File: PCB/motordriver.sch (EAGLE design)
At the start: 52 parts, among them IC1 7818TV

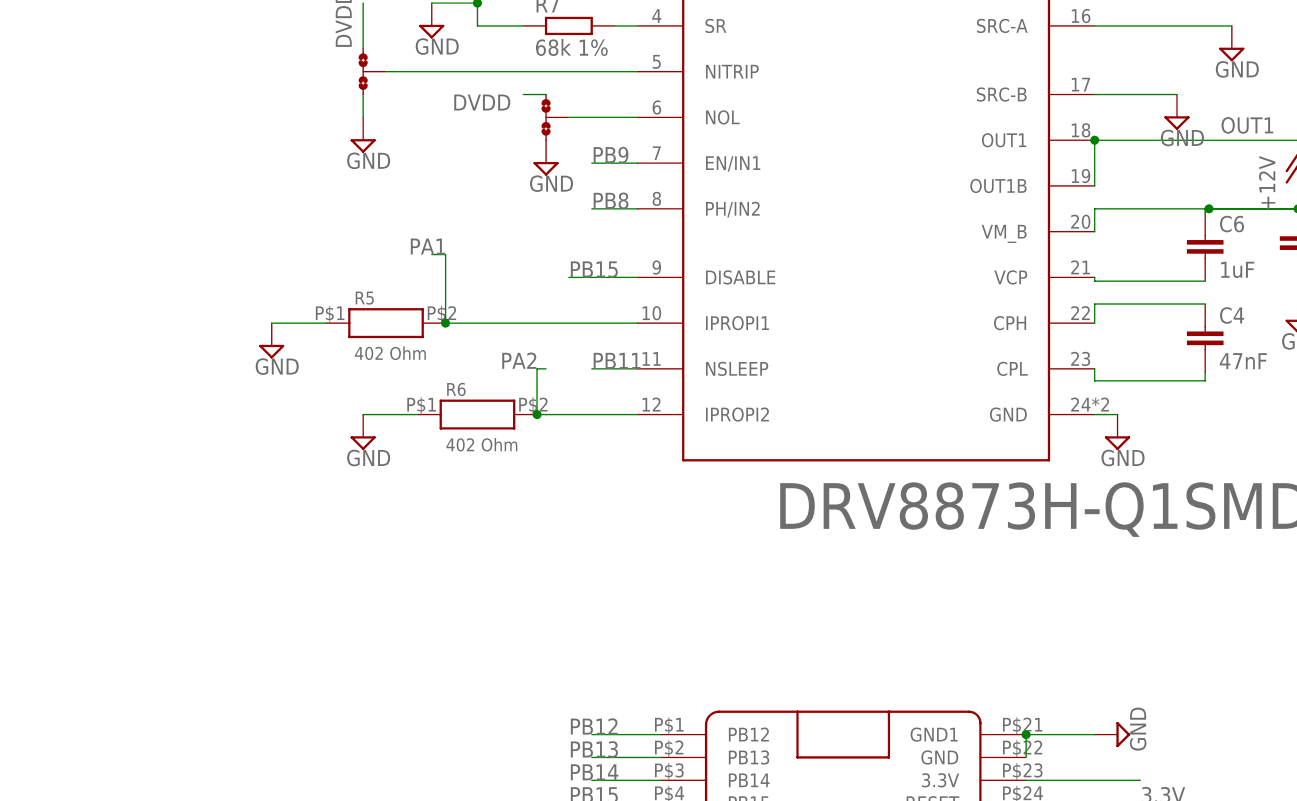
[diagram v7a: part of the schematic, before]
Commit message: added Low pass rc filter for the IOPROPx output
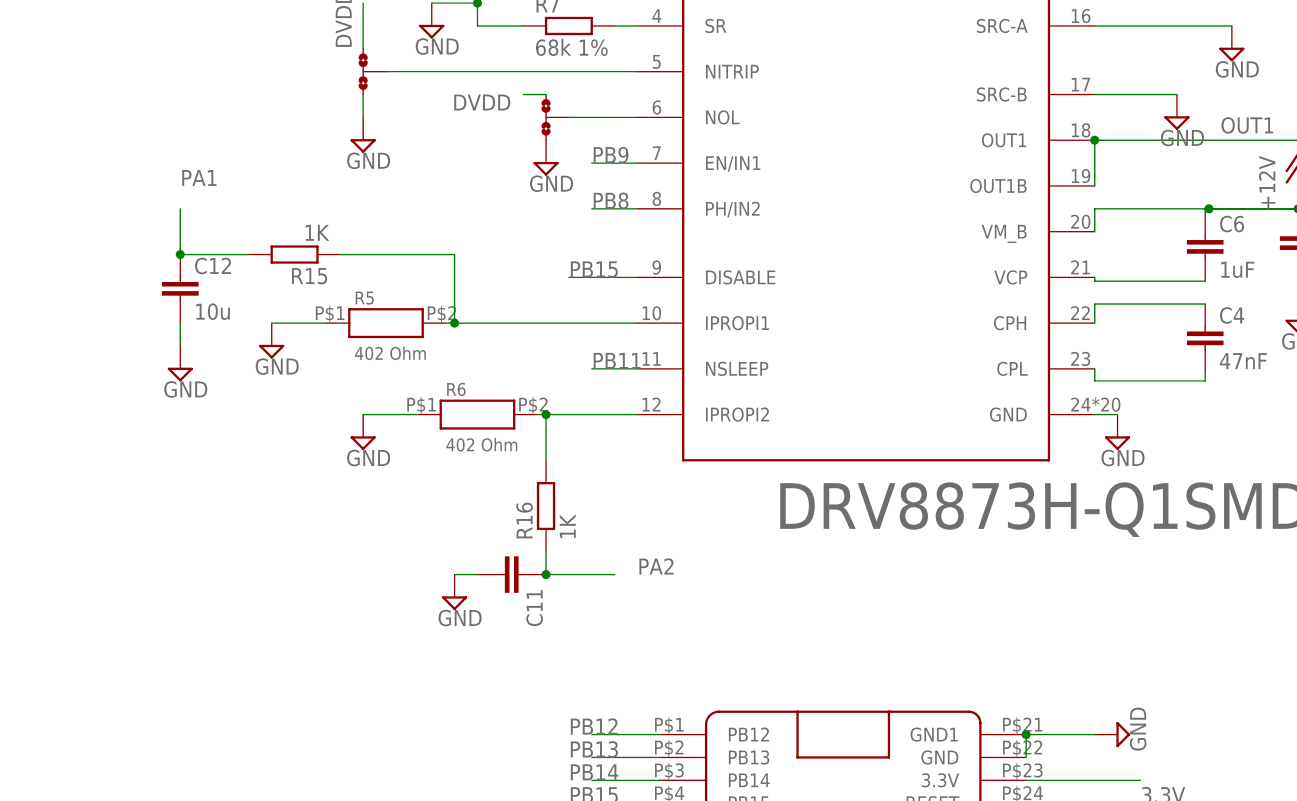
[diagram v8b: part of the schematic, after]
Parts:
- added C11: (no value), rcl:C-EUC0805K
- added C12: 10u, rcl:C-EUC0805K
- added R15, R16: 1K, resistor:R-EU_R0805
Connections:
- new net N$100: R15.1, R5.P$2, U$2.IPROPI1
- new net N$101: R16.2, R6.P$2, U$2.IPROPI2
- net GND: now also C11.2, C12.2
- net PA1: now also C12.1, R15.2; no longer R5.P$2, U$2.IPROPI1
- net PA2: now also C11.1, R16.1; no longer R6.P$2, U$2.IPROPI2
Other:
- moved on the sheet: U$2
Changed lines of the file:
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@@
 <part name="C10" library="rcl" library_urn="urn:adsk.eagle:library:334" deviceset="C-EU" device="C0805K" package3d_urn="urn:adsk.eagle:package:23681/2" value="100nF"/>
 <part name="SUPPLY25" library="supply2" library_urn="urn:adsk.eagle:library:372" deviceset="GND" device=""/>
+<part name="R15" library="resistor" library_urn="urn:adsk.eagle:library:348" deviceset="R-EU_" device="R0805" package3d_urn="urn:adsk.eagle:package:26059/1" value="1K"/>
+<part name="R16" library="resistor" library_urn="urn:adsk.eagle:library:348" deviceset="R-EU_" device="R0805" package3d_urn="urn:adsk.eagle:package:26059/1" value="1K"/>
+<part name="C11" library="rcl" library_urn="urn:adsk.eagle:library:334" deviceset="C-EU" device="C0805K" package3d_urn="urn:adsk.eagle:package:23681/2"/>
+<part name="C12" library="rcl" library_urn="urn:adsk.eagle:library:334" deviceset="C-EU" device="C0805K" package3d_urn="urn:adsk.eagle:package:23681/2" value="10u"/>
+<part name="SUPPLY26" library="supply2" library_urn="urn:adsk.eagle:library:372" deviceset="GND" device=""/>
+<part name="SUPPLY27" library="supply2" library_urn="urn:adsk.eagle:library:372" deviceset="GND" device=""/>
 </parts>
 <sheets>
@@
 <instance part="C10" gate="G$1" x="113.792" y="93.98"/>
 <instance part="SUPPLY25" gate="GND" x="113.792" y="83.058"/>
+<instance part="R15" gate="G$1" x="83.82" y="193.04" rot="R180"/>
+<instance part="R16" gate="G$1" x="111.76" y="165.1" rot="R90"/>
+<instance part="C11" gate="G$1" x="109.22" y="157.48" rot="R270"/>
+<instance part="C12" gate="G$1" x="71.12" y="190.5"/>
+<instance part="SUPPLY26" gate="GND" x="71.12" y="180.34"/>
+<instance part="SUPPLY27" gate="GND" x="101.6" y="154.94"/>
 </instances>
 <busses>
@@
 <pinref part="SUPPLY25" gate="GND" pin="GND"/>
 <wire x1="113.792" y1="85.598" x2="113.792" y2="88.9" width="0.1524" layer="91"/>
+</segment>
+<segment>
+<pinref part="SUPPLY26" gate="GND" pin="GND"/>
+<pinref part="C12" gate="G$1" pin="2"/>
+<wire x1="71.12" y1="182.88" x2="71.12" y2="185.42" width="0.1524" layer="91"/>
+</segment>
+<segment>
+<pinref part="SUPPLY27" gate="GND" pin="GND"/>
+<pinref part="C11" gate="G$1" pin="2"/>
+<wire x1="101.6" y1="157.48" x2="104.14" y2="157.48" width="0.1524" layer="91"/>
 </segment>
 </net>
@@
 </segment>
 <segment>
-<pinref part="U$2" gate="G$1" pin="IPROPI1"/>
-<pinref part="R5" gate="G$1" pin="P$2"/>
-<wire x1="121.92" y1="185.42" x2="100.6" y2="185.42" width="0.1524" layer="91"/>
-<wire x1="100.6" y1="185.42" x2="100.6" y2="193.04" width="0.1524" layer="91"/>
-<wire x1="100.6" y1="193.04" x2="99.06" y2="193.04" width="0.1524" layer="91"/>
-<junction x="100.6" y="185.42"/>
-<label x="96.52" y="193.04" size="1.778" layer="95"/>
+<pinref part="R15" gate="G$1" pin="2"/>
+<pinref part="C12" gate="G$1" pin="1"/>
+<wire x1="78.74" y1="193.04" x2="71.12" y2="193.04" width="0.1524" layer="91"/>
+<wire x1="71.12" y1="193.04" x2="71.12" y2="198.12" width="0.1524" layer="91"/>
+<junction x="71.12" y="193.04"/>
+<label x="71.12" y="200.66" size="1.778" layer="95"/>
 </segment>
 </net>
@@
 <net name="PA2" class="0">
 <segment>
-<pinref part="U$2" gate="G$1" pin="IPROPI2"/>
-<pinref part="R6" gate="G$1" pin="P$2"/>
-<wire x1="121.92" y1="175.26" x2="110.76" y2="175.26" width="0.1524" layer="91"/>
-<wire x1="110.76" y1="175.26" x2="110.76" y2="180.34" width="0.1524" layer="91"/>
-<wire x1="110.76" y1="180.34" x2="111.76" y2="180.34" width="0.1524" layer="91"/>
-<junction x="110.76" y="175.26"/>
-<label x="106.68" y="180.34" size="1.778" layer="95"/>
-</segment>
-<segment>
 <pinref part="U$1" gate="G$1" pin="PA2"/>
 <wire x1="165.1" y1="106.68" x2="170.18" y2="106.68" width="0.1524" layer="91"/>
@@
 <wire x1="180.34" y1="109.22" x2="180.34" y2="106.68" width="0.1524" layer="91"/>
 <wire x1="180.34" y1="106.68" x2="170.18" y2="106.68" width="0.1524" layer="91"/>
+</segment>
+<segment>
+<pinref part="C11" gate="G$1" pin="1"/>
+<pinref part="R16" gate="G$1" pin="1"/>
+<wire x1="111.76" y1="157.48" x2="111.76" y2="160.02" width="0.1524" layer="91"/>
+<wire x1="119.38" y1="157.48" x2="111.76" y2="157.48" width="0.1524" layer="91"/>
+<junction x="111.76" y="157.48"/>
+<label x="121.92" y="157.48" size="1.778" layer="95"/>
 </segment>
 </net>
@@
 </segment>
 </net>
+<net name="N$100" class="0">
+<segment>
+<pinref part="U$2" gate="G$1" pin="IPROPI1"/>
+<pinref part="R5" gate="G$1" pin="P$2"/>
+<wire x1="121.92" y1="185.42" x2="101.6" y2="185.42" width="0.1524" layer="91"/>
+<pinref part="R15" gate="G$1" pin="1"/>
+<wire x1="101.6" y1="185.42" x2="100.6" y2="185.42" width="0.1524" layer="91"/>
+<wire x1="88.9" y1="193.04" x2="101.6" y2="193.04" width="0.1524" layer="91"/>
+<wire x1="101.6" y1="193.04" x2="101.6" y2="185.42" width="0.1524" layer="91"/>
+<junction x="101.6" y="185.42"/>
+</segment>
+</net>
+<net name="N$101" class="0">
+<segment>
+<pinref part="U$2" gate="G$1" pin="IPROPI2"/>
+<pinref part="R6" gate="G$1" pin="P$2"/>
+<wire x1="121.92" y1="175.26" x2="111.76" y2="175.26" width="0.1524" layer="91"/>
+<pinref part="R16" gate="G$1" pin="2"/>
+<wire x1="111.76" y1="175.26" x2="110.76" y2="175.26" width="0.1524" layer="91"/>
+<wire x1="111.76" y1="170.18" x2="111.76" y2="175.26" width="0.1524" layer="91"/>
+<junction x="111.76" y="175.26"/>
+</segment>
+</net>
